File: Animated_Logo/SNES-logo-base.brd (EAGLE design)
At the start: 16.2 x 26 mm, 21 parts, among them IC1 TINY10S, Q1 BC848ALT1SMD, Q2 BC848ALT1SMD, Q3 BC848ALT1SMD, Q4 BC848ALT1SMD

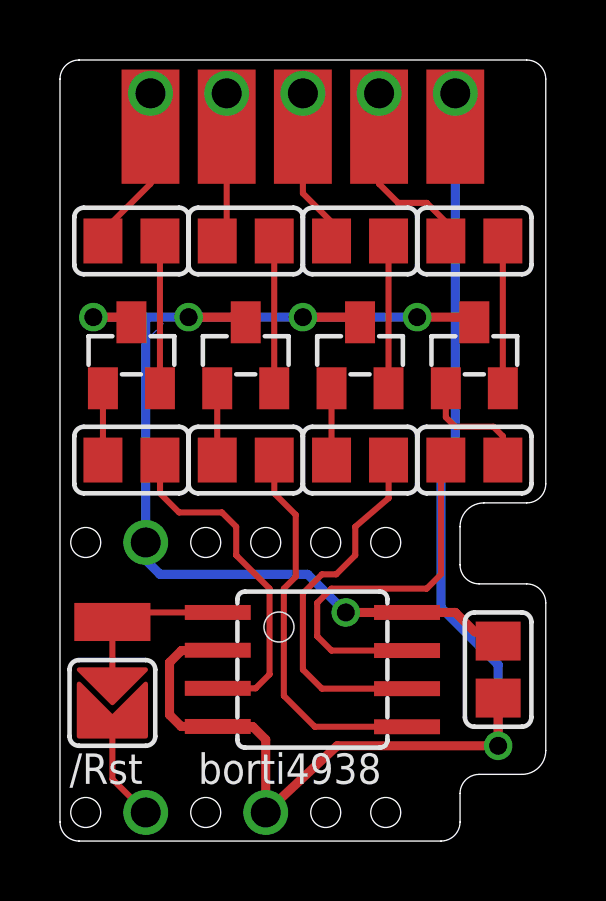
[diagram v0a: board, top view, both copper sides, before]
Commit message: Minor updates for the Logo-PCBs: - move resistors for LEDs to the LED PCB - LEDs can be either in 0805 or P-LCC-2 package
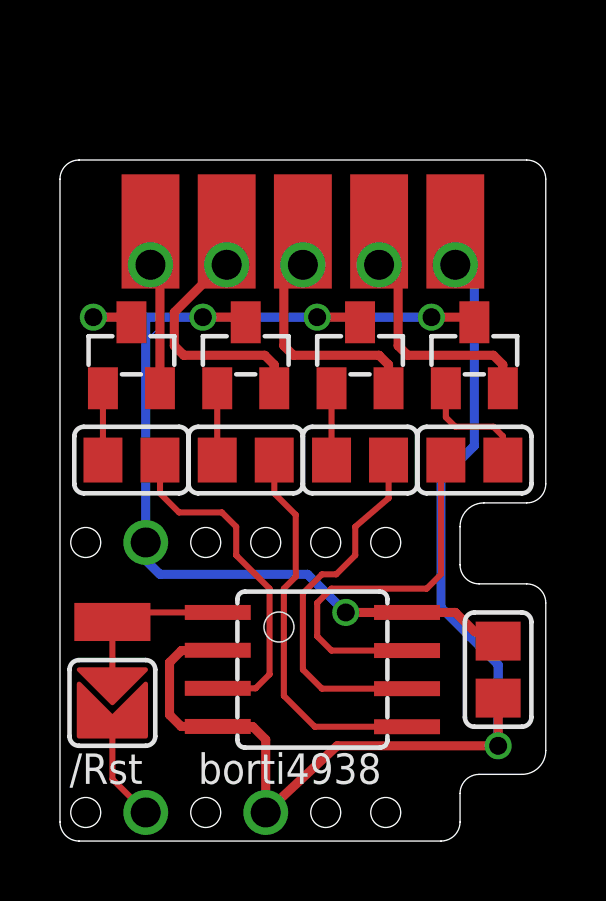
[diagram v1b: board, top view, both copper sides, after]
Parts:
- removed R2, R4: 150, snes_div:Z0805
- removed R6, R8: 100, snes_div:Z0805
- moved U$11 3.49 mm to (3.02, 20.3), turned to 180 degrees
- moved U$12 3.49 mm to (10.6, 20.3), turned to 180 degrees
- moved U$13 3.49 mm to (8.10, 20.3), turned to 180 degrees
- moved U$14 3.49 mm to (5.56, 20.3), turned to 180 degrees
- moved U$15 3.49 mm to (13.2, 20.3), turned to 180 degrees
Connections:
- removed net N$10: Q3.2, R6.1
- removed net N$11: Q4.2, R8.1
- removed net N$16: R2.2, U$11.P$1, U$11.P$2
- removed net N$17: R4.2, U$12.P$1, U$12.P$2
- removed net N$18: R6.2, U$13.P$1, U$13.P$2
- removed net N$19: R8.2, U$14.P$1, U$14.P$2
- new net N$1: Q2.2, U$12.P$1, U$12.P$2
- new net N$3: Q3.2, U$13.P$1, U$13.P$2
- net N$8: now also Q4.2, U$14.P$1, U$14.P$2; no longer Q1.2, R2.1
- net N$9: now also Q1.2, U$11.P$1, U$11.P$2; no longer Q2.2, R4.1
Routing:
- net N$3: track 0.00 -> 8.98 mm
- net N$1: track 0.00 -> 8.70 mm
- net N$17: track 7.51 -> 0.00 mm
- net N$16: track 6.63 -> 0.00 mm
- net N$18: track 6.43 -> 0.00 mm
- net N$19: track 6.16 -> 0.00 mm
- net GND: track 44.5 -> 39.3 mm
- net N$11: track 4.91 -> 0.00 mm
- net N$10: track 4.91 -> 0.00 mm
- net N$8: track 4.91 -> 8.97 mm
- net VCC: track 42.8 -> 43.8 mm
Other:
- board size 16.2 x 26 mm -> 16.2 x 22.7 mm
- board text removed: "R180|2xR120|R180"
